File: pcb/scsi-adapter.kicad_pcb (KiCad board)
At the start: 4 copper layers, 0 parts

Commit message: basic pcb layout
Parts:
- added C1001: 22pF C0G, Capacitor_SMD:C_0402_1005Metric, F.Cu at (101.4, 209.3)
- added C1002: 100nF 50V, Capacitor_SMD:C_0402_1005Metric, F.Cu at (104.3, 209.3)
- added C101: 1uF 50V X7R, Capacitor_SMD:C_0805_2012Metric, F.Cu at (102.2, 173.0)
- added C102: 100nF 50V, Capacitor_SMD:C_0402_1005Metric, F.Cu at (105.9, 172.5)
- added C103: 2.2nF, Capacitor_SMD:C_0402_1005Metric, F.Cu at (108.8, 172.5)
- added C104: 1nF, Capacitor_SMD:C_0402_1005Metric, F.Cu at (111.6, 172.5)
- added C105: 1uF 25V, Capacitor_SMD:C_0402_1005Metric, F.Cu at (114.5, 172.5)
- added C106: 1uF 25V, Capacitor_SMD:C_0402_1005Metric, F.Cu at (117.4, 172.5)
- added C107: 4.7uF 25V, Capacitor_SMD:C_0805_2012Metric, F.Cu at (121.0, 173.0)
- added C108: 100nF 50V, Capacitor_SMD:C_0402_1005Metric, F.Cu at (124.7, 172.5)
- added C109: 22uF 25V, Capacitor_SMD:C_0805_2012Metric, F.Cu at (128.3, 173.0)
- added C110: 1uF 25V, Capacitor_SMD:C_0402_1005Metric, F.Cu at (132.0, 172.5)
- added C1101: 22pF C0G, Capacitor_SMD:C_0402_1005Metric, F.Cu at (107.2, 209.3)
- added C1102: 100nF 50V, Capacitor_SMD:C_0402_1005Metric, F.Cu at (110.0, 209.3)
- added C111: 10uF 25V, Capacitor_SMD:C_0805_2012Metric, F.Cu at (135.7, 173.0)
- added C112: 1uF 25V, Capacitor_SMD:C_0402_1005Metric, F.Cu at (139.3, 172.5)
- added C113: 10uF 25V, Capacitor_SMD:C_0805_2012Metric, F.Cu at (143.0, 173.0)
- added C1201: 22pF C0G, Capacitor_SMD:C_0402_1005Metric, F.Cu at (112.9, 209.3)
- added C1202: 100nF 50V, Capacitor_SMD:C_0402_1005Metric, F.Cu at (115.8, 209.3)
- added C1301: 22pF C0G, Capacitor_SMD:C_0402_1005Metric, F.Cu at (118.7, 209.3)
- added C1302: 100nF 50V, Capacitor_SMD:C_0402_1005Metric, F.Cu at (121.5, 209.3)
- added C1401: 22pF C0G, Capacitor_SMD:C_0402_1005Metric, F.Cu at (124.4, 209.3)
- added C1402: 100nF 50V, Capacitor_SMD:C_0402_1005Metric, F.Cu at (127.3, 209.3)
- added C1501: 22pF C0G, Capacitor_SMD:C_0402_1005Metric, F.Cu at (130.1, 209.3)
- added C1502: 100nF 50V, Capacitor_SMD:C_0402_1005Metric, F.Cu at (133.0, 209.3)
- added C1601: 22pF C0G, Capacitor_SMD:C_0402_1005Metric, F.Cu at (135.9, 209.3)
- added C1602: 100nF 50V, Capacitor_SMD:C_0402_1005Metric, F.Cu at (138.7, 209.3)
- added C1701: 22pF C0G, Capacitor_SMD:C_0402_1005Metric, F.Cu at (141.6, 209.3)
- added C1702: 100nF 50V, Capacitor_SMD:C_0402_1005Metric, F.Cu at (144.5, 209.3)
- added C1801: 22pF C0G, Capacitor_SMD:C_0402_1005Metric, F.Cu at (147.4, 209.3)
- added C1802: 100nF 50V, Capacitor_SMD:C_0402_1005Metric, F.Cu at (150.2, 209.3)
- added C1901: 22pF C0G, Capacitor_SMD:C_0402_1005Metric, F.Cu at (153.1, 209.3)
- added C1902: 100nF 50V, Capacitor_SMD:C_0402_1005Metric, F.Cu at (156.0, 209.3)
- added C2001: 22pF C0G, Capacitor_SMD:C_0402_1005Metric, F.Cu at (158.8, 209.3)
- added C2002: 100nF 50V, Capacitor_SMD:C_0402_1005Metric, F.Cu at (161.7, 209.3)
- added C201: 1uF 25V, Capacitor_SMD:C_0402_1005Metric, F.Cu at (101.4, 305.5)
- added C202: 1uF 25V, Capacitor_SMD:C_0402_1005Metric, F.Cu at (104.3, 305.5)
- added C203: 100nF 50V, Capacitor_SMD:C_0402_1005Metric, F.Cu at (107.2, 305.5)
- added C204: 2.2nF, Capacitor_SMD:C_0402_1005Metric, F.Cu at (110.0, 305.5)
- added C205: 1nF, Capacitor_SMD:C_0402_1005Metric, F.Cu at (112.9, 305.5)
- added C206: 100nF 50V, Capacitor_SMD:C_0402_1005Metric, F.Cu at (115.8, 305.5)
- added C207: 1uF 25V, Capacitor_SMD:C_0402_1005Metric, F.Cu at (118.7, 305.5)
- added C2101: 22pF C0G, Capacitor_SMD:C_0402_1005Metric, F.Cu at (164.6, 209.3)
- added C2102: 100nF 50V, Capacitor_SMD:C_0402_1005Metric, F.Cu at (167.4, 209.3)
- added C2202: 100nF 50V, Capacitor_SMD:C_0402_1005Metric, F.Cu at (170.3, 209.3)
- added C2301: 22pF C0G, Capacitor_SMD:C_0402_1005Metric, F.Cu at (173.2, 209.3)
- added C2302: 100nF 50V, Capacitor_SMD:C_0402_1005Metric, F.Cu at (176.1, 209.3)
- added C2402: 100nF 50V, Capacitor_SMD:C_0402_1005Metric, F.Cu at (178.9, 209.3)
- added C2502: 100nF 50V, Capacitor_SMD:C_0402_1005Metric, F.Cu at (181.8, 209.3)
- added C2602: 100nF 50V, Capacitor_SMD:C_0402_1005Metric, F.Cu at (184.7, 209.3)
- added C301: 100nF 50V, Capacitor_SMD:C_0402_1005Metric, F.Cu at (187.5, 209.3)
- added C302: 100nF 50V, Capacitor_SMD:C_0402_1005Metric, F.Cu at (190.4, 209.3)
- added C303: 100nF 50V, Capacitor_SMD:C_0402_1005Metric, F.Cu at (193.3, 209.3)
- added C401: 4.7uF 10V, Capacitor_SMD:C_0402_1005Metric, F.Cu at (146.0, 61.7)
- added C402: 4.7uF 10V, scsi-adapter:C_0402_1005Metric_Wide, F.Cu at (147.8, 63.0)
- added C403: 4.7uF 10V, scsi-adapter:C_0402_1005Metric_Wide, F.Cu at (147.2, 63.6)
- added C404: 4.7uF 10V, Capacitor_SMD:C_0402_1005Metric, F.Cu at (158.0, 52.8)
- added C405: 10uF 25V, Capacitor_SMD:C_0805_2012Metric, F.Cu at (140.1, 62.2)
- added C406: 100nF, Capacitor_SMD:C_0402_1005Metric, F.Cu at (157.9, 68.5)
- added C407: 100nF, Capacitor_SMD:C_0402_1005Metric, F.Cu at (161.5, 64.9)
- added C408: 100nF, Capacitor_SMD:C_0402_1005Metric, F.Cu at (162.3, 59.4)
- added C409: 100nF, Capacitor_SMD:C_0402_1005Metric, F.Cu at (161.0, 55.9)
- added C410: 100nF, Capacitor_SMD:C_0402_1005Metric, F.Cu at (152.1, 52.3)
- added C411: 100nF, Capacitor_SMD:C_0402_1005Metric, F.Cu at (148.9, 54.8)
- added C412: 100nF, Capacitor_SMD:C_0402_1005Metric, F.Cu at (145.9, 58.5)
- added C413: 100nF, Capacitor_SMD:C_0402_1005Metric, F.Cu at (152.6, 70.6)
- added C414: 100nF, Capacitor_SMD:C_0402_1005Metric, F.Cu at (159.8, 66.6)
- added C415: 100nF, Capacitor_SMD:C_0402_1005Metric, F.Cu at (159.1, 53.9)
- added C416: 100nF, Capacitor_SMD:C_0402_1005Metric, F.Cu at (148.2, 55.5)
- added C417: 100nF, Capacitor_SMD:C_0402_1005Metric, F.Cu at (146.6, 57.8)
- added C418: 100nF, Capacitor_SMD:C_0402_1005Metric, F.Cu at (148.7, 67.7)
- added C419: 15pF, Capacitor_SMD:C_0402_1005Metric, F.Cu at (162.6, 54.4)
- added C420: 15pF, Capacitor_SMD:C_0402_1005Metric, F.Cu at (160.5, 52.3)
- added C421: 100nF, Capacitor_SMD:C_0402_1005Metric, F.Cu at (143.9, 73.2)
- added C422: 100nF, Capacitor_SMD:C_0402_1005Metric, F.Cu at (139.9, 80.2)
- added C423: 1uF 25V, Capacitor_SMD:C_0402_1005Metric, F.Cu at (140.7, 80.9)
- added C424: 100nF, Capacitor_SMD:C_0402_1005Metric, F.Cu at (168.6, 191.0)
- added C501: 100nF, Capacitor_SMD:C_0402_1005Metric, F.Cu at (101.4, 148.3)
- added C502: 10uF 25V, Capacitor_SMD:C_0805_2012Metric, F.Cu at (105.1, 148.9)
- added C503: 100nF, Capacitor_SMD:C_0402_1005Metric, F.Cu at (108.8, 148.3)
- added C601: 10uF 25V, Capacitor_SMD:C_0805_2012Metric, F.Cu at (102.2, 319.1)
- added C602: 100nF, Capacitor_SMD:C_0402_1005Metric, F.Cu at (105.9, 318.6)
- added C603: 100nF, Capacitor_SMD:C_0402_1005Metric, F.Cu at (108.8, 318.6)
- added C604: DNP, Capacitor_SMD:C_0402_1005Metric, F.Cu at (111.6, 318.6)
- added C605: DNP, Capacitor_SMD:C_0402_1005Metric, F.Cu at (114.5, 318.6)
- added C701: 4.7uF 10V, Capacitor_SMD:C_0402_1005Metric, F.Cu at (101.4, 131.0)
- added C702: 100nF, Capacitor_SMD:C_0402_1005Metric, F.Cu at (104.3, 131.0)
- added C703: 4.7uF 10V, Capacitor_SMD:C_0402_1005Metric, F.Cu at (107.2, 131.0)
- added C704: 100nF, Capacitor_SMD:C_0402_1005Metric, F.Cu at (110.0, 131.0)
- added C705: 100nF, Capacitor_SMD:C_0402_1005Metric, F.Cu at (112.9, 131.0)
- added C706: 100nF, Capacitor_SMD:C_0402_1005Metric, F.Cu at (115.8, 131.0)
- added C707: 100nF, Capacitor_SMD:C_0402_1005Metric, F.Cu at (118.7, 131.0)
- added C708: 100nF, Capacitor_SMD:C_0402_1005Metric, F.Cu at (121.5, 131.0)
- added C709: 4.7uF, Capacitor_SMD:C_0402_1005Metric, F.Cu at (124.4, 131.0)
- added C710: 100nF, Capacitor_SMD:C_0402_1005Metric, F.Cu at (127.3, 131.0)
- added C711: 4.7uF, Capacitor_SMD:C_0402_1005Metric, F.Cu at (130.1, 131.0)
- added C712: 100nF, Capacitor_SMD:C_0402_1005Metric, F.Cu at (133.0, 131.0)
- added C713: 100nF, Capacitor_SMD:C_0402_1005Metric, F.Cu at (135.9, 131.0)
- added C714: 100nF, Capacitor_SMD:C_0402_1005Metric, F.Cu at (138.7, 131.0)
- added C715: 15pF, Capacitor_SMD:C_0402_1005Metric, F.Cu at (141.6, 131.0)
- added C716: 15pF, Capacitor_SMD:C_0402_1005Metric, F.Cu at (144.5, 131.0)
- added C717: 10nF, Capacitor_SMD:C_0402_1005Metric, F.Cu at (147.4, 131.0)
- added C901: 22pF C0G, Capacitor_SMD:C_0402_1005Metric, F.Cu at (196.1, 209.3)
- added C902: 100nF 50V, Capacitor_SMD:C_0402_1005Metric, F.Cu at (199.0, 209.3)
- added D101: SMF15CA, Diode_SMD:D_SOD-123F, F.Cu at (148.0, 173.2)
- added D102: BZT52C5V6, Diode_SMD:D_SOD-123, F.Cu at (153.6, 173.2)
- added D201: KT-0603R red, LED_SMD:LED_0603_1608Metric, F.Cu at (122.1, 305.8)
- added D202: KT-0805Y yellow, LED_SMD:LED_0805_2012Metric, F.Cu at (126.4, 306.0)
- added D203: SS14, Diode_SMD:D_SMA, F.Cu at (132.7, 306.8)
- added D204: SMF6.0A, Diode_SMD:D_SOD-123F, F.Cu at (139.5, 306.2)
- added D301: H5VUD5BB, Diode_SMD:D_SOD-523, F.Cu at (202.3, 209.5)
- added D302: H5VUD5BB, Diode_SMD:D_SOD-523, F.Cu at (205.9, 209.5)
- added D303: H5VUD5BB, Diode_SMD:D_SOD-523, F.Cu at (209.5, 209.5)
- added D304: H5VUD5BB, Diode_SMD:D_SOD-523, F.Cu at (213.1, 209.5)
- added D305: H5VUD5BB, Diode_SMD:D_SOD-523, F.Cu at (216.7, 209.5)
- added D306: H5VUD5BB, Diode_SMD:D_SOD-523, F.Cu at (220.2, 209.5)
- added D307: H5VUD5BB, Diode_SMD:D_SOD-523, F.Cu at (223.8, 209.5)
- added D308: H5VUD5BB, Diode_SMD:D_SOD-523, F.Cu at (227.4, 209.5)
- added D309: H5VUD5BB, Diode_SMD:D_SOD-523, F.Cu at (231.0, 209.5)
- added D310: H5VUD5BB, Diode_SMD:D_SOD-523, F.Cu at (234.6, 209.5)
- added D311: H5VUD5BB, Diode_SMD:D_SOD-523, F.Cu at (238.2, 209.5)
- added D312: H5VUD5BB, Diode_SMD:D_SOD-523, F.Cu at (241.8, 209.5)
- added D313: H5VUD5BB, Diode_SMD:D_SOD-523, F.Cu at (245.4, 209.5)
- added D314: H5VUD5BB, Diode_SMD:D_SOD-523, F.Cu at (249.0, 209.5)
- added D315: H5VUD5BB, Diode_SMD:D_SOD-523, F.Cu at (252.6, 209.5)
- added D316: H5VUD5BB, Diode_SMD:D_SOD-523, F.Cu at (256.2, 209.5)
- added D317: H5VUD5BB, Diode_SMD:D_SOD-523, F.Cu at (259.8, 209.5)
- added D318: H5VUD5BB, Diode_SMD:D_SOD-523, F.Cu at (263.4, 209.5)
- added D501: KT-0805Y yellow, LED_SMD:LED_0805_2012Metric, F.Cu at (112.4, 148.9)
- added D502: KT-0603R red, LED_SMD:LED_0603_1608Metric, F.Cu at (116.7, 148.6)
- added D503: KT-0603R red, LED_SMD:LED_0603_1608Metric, F.Cu at (120.7, 148.6)
- added D504: KT-0805Y yellow, LED_SMD:LED_0805_2012Metric, F.Cu at (125.0, 148.9)
- added D505: KT-0805G green, LED_SMD:LED_0805_2012Metric, F.Cu at (129.4, 148.9)
- added D601: H5VUD5BB, Diode_SMD:D_SOD-523, F.Cu at (117.8, 318.9)
- added D602: H5VUD5BB, Diode_SMD:D_SOD-523, F.Cu at (121.3, 318.9)
- added D603: H7VL10B, Diode_SMD:D_0402_1005Metric, F.Cu at (124.8, 318.6)
- added D604: H7VL10B, Diode_SMD:D_0402_1005Metric, F.Cu at (128.0, 318.6)
- added D605: SMF6.0A, Diode_SMD:D_SOD-123F, F.Cu at (132.2, 319.3)
- added D606: 1N5819WS, Diode_SMD:D_SOD-323, F.Cu at (137.1, 319.1)
- added D607: KT-0805G green, LED_SMD:LED_0805_2012Metric, F.Cu at (141.4, 319.1)
- added FB701: 600R@100MHz, Inductor_SMD:L_0603_1608Metric, F.Cu at (150.8, 131.3)
- added FB702: 600R@100MHz, Inductor_SMD:L_0603_1608Metric, F.Cu at (154.8, 131.3)
- added H1: M3, MountingHole_3.2mm_M3, F.Cu at (104.0, 34.0)
- added H2: M3, MountingHole_3.2mm_M3, F.Cu at (216.0, 34.0)
- added H3: M3, MountingHole_3.2mm_M3, F.Cu at (216.0, 116.0)
- added H4: M3, MountingHole_3.2mm_M3, F.Cu at (104.0, 116.0)
- added J101: Bench 5V, scsi-adapter:TerminalBlock_Kangnex_WJ500V-5.08-2P_1x02_P5.08mm_Horizontal, F.Cu at (105.5, 102.7)
- added J201: TERMPWR jumper, Connector_PinHeader_2.54mm:PinHeader_1x02_P2.54mm_Vertical, F.Cu at (136.0, 111.2)
- added J301: IDC50 box header, Connector_IDC:IDC-Header_2x25_P2.54mm_Vertical, F.Cu at (143.9, 114.3)
- added J302: HD50 female R/A, scsi-adapter:TE_AMPLIMITE-050_5787082-5_50pos_P1.27mm_Horizontal, F.Cu at (210.6, 59.8)
- added J303: 2x17 box header, Connector_IDC:IDC-Header_2x17_P2.54mm_Vertical, F.Cu at (204.9, 35.7)
- added J401: TC2030-IDC, Connector:Tag-Connect_TC2030-IDC-FP_2x03_P1.27mm_Vertical, F.Cu at (149.5, 39.0)
- added J501: TF PUSH, scsi-adapter:microSD_SHOUHAN_TF-PUSH_PushPush_CardDetect, F.Cu at (127.5, 34.0)
- added J601: USB-C (HRO TYPE-C-31-M-12), Connector_USB:USB_C_Receptacle_HRO_TYPE-C-31-M-12, F.Cu at (103.2, 75.0)
- added L401: 3.3uH, scsi-adapter:L_Abracon_AOTA-B201610_2.0x1.6mm_Polarized, F.Cu at (146.0, 64.8)
- added Q1001: FDV301N, Package_TO_SOT_SMD:SOT-23, F.Cu at (65.4, 151.9)
- added Q1101: FDV301N, Package_TO_SOT_SMD:SOT-23, F.Cu at (102.5, 283.7)
- added Q1201: FDV301N, Package_TO_SOT_SMD:SOT-23, F.Cu at (107.4, 283.7)
- added Q1301: FDV301N, Package_TO_SOT_SMD:SOT-23, F.Cu at (112.3, 283.7)
- added Q1401: FDV301N, Package_TO_SOT_SMD:SOT-23, F.Cu at (117.2, 283.7)
- added Q1501: FDV301N, Package_TO_SOT_SMD:SOT-23, F.Cu at (122.1, 283.7)
- added Q1601: FDV301N, Package_TO_SOT_SMD:SOT-23, F.Cu at (127.0, 283.7)
- added Q1701: FDV301N, Package_TO_SOT_SMD:SOT-23, F.Cu at (131.9, 283.7)
- added Q1801: FDV301N, Package_TO_SOT_SMD:SOT-23, F.Cu at (136.8, 283.7)
- added Q1901: FDV301N, Package_TO_SOT_SMD:SOT-23, F.Cu at (141.7, 283.7)
- added Q2001: FDV301N, Package_TO_SOT_SMD:SOT-23, F.Cu at (146.6, 283.7)
- added Q201: 2N7002, Package_TO_SOT_SMD:SOT-23, F.Cu at (149.2, 306.7)
- added Q2101: FDV301N, Package_TO_SOT_SMD:SOT-23, F.Cu at (151.6, 283.7)
- added Q2301: FDV301N, Package_TO_SOT_SMD:SOT-23, F.Cu at (156.5, 283.7)
- added Q901: FDV301N, Package_TO_SOT_SMD:SOT-23, F.Cu at (161.4, 283.7)
- added R1001: 100R, Resistor_SMD:R_0402_1005Metric, F.Cu at (165.3, 282.5)
- added R1002: 4.7k, Resistor_SMD:R_0402_1005Metric, F.Cu at (168.2, 282.5)
- added R1003: 100R, Resistor_SMD:R_0402_1005Metric, F.Cu at (171.1, 282.5)
- added R101: 510k, Resistor_SMD:R_0402_1005Metric, F.Cu at (170.8, 172.5)
- added R102: 39k, Resistor_SMD:R_0402_1005Metric, F.Cu at (173.7, 172.5)
- added R103: 3.9k, Resistor_SMD:R_0402_1005Metric, F.Cu at (176.6, 172.5)
- added R104: 150k, Resistor_SMD:R_0402_1005Metric, F.Cu at (179.5, 172.5)
- added R105: 10k, Resistor_SMD:R_0402_1005Metric, F.Cu at (182.4, 172.5)
- added R106: 1.5k, Resistor_SMD:R_0402_1005Metric, F.Cu at (185.3, 172.5)
- added R107: 100k, Resistor_SMD:R_0402_1005Metric, F.Cu at (188.2, 172.5)
- added R108: 39k, Resistor_SMD:R_0402_1005Metric, F.Cu at (191.1, 172.5)
- added R109: 10k, Resistor_SMD:R_0402_1005Metric, F.Cu at (194.0, 172.5)
- added R110: 1R, Resistor_SMD:R_0603_1608Metric, F.Cu at (197.5, 172.7)
- added R1101: 100R, Resistor_SMD:R_0402_1005Metric, F.Cu at (174.0, 282.5)
- added R1102: 4.7k, Resistor_SMD:R_0402_1005Metric, F.Cu at (176.9, 282.5)
- added R1103: 100R, Resistor_SMD:R_0402_1005Metric, F.Cu at (179.8, 282.5)
- added R111: 100k, Resistor_SMD:R_0402_1005Metric, F.Cu at (201.0, 172.5)
- added R112: 75k, Resistor_SMD:R_0402_1005Metric, F.Cu at (203.9, 172.5)
- added R113: 47k, Resistor_SMD:R_0402_1005Metric, F.Cu at (206.8, 172.5)
- added R114: 27k, Resistor_SMD:R_0402_1005Metric, F.Cu at (209.7, 172.5)
- added R115: 1M, Resistor_SMD:R_0603_1608Metric, F.Cu at (213.2, 172.7)
- added R116: 100k, Resistor_SMD:R_0402_1005Metric, F.Cu at (216.6, 172.5)
- added R117: 75k, Resistor_SMD:R_0402_1005Metric, F.Cu at (219.5, 172.5)
- added R118: 39k, Resistor_SMD:R_0402_1005Metric, F.Cu at (222.4, 172.5)
- added R119: 5.6k, Resistor_SMD:R_0402_1005Metric, F.Cu at (225.3, 172.5)
- added R120: 33k, Resistor_SMD:R_0402_1005Metric, F.Cu at (228.3, 172.5)
- added R1201: 100R, Resistor_SMD:R_0402_1005Metric, F.Cu at (182.7, 282.5)
- added R1202: 4.7k, Resistor_SMD:R_0402_1005Metric, F.Cu at (185.7, 282.5)
- added R1203: 100R, Resistor_SMD:R_0402_1005Metric, F.Cu at (188.6, 282.5)
- added R121: 270R, Resistor_SMD:R_0603_1608Metric, F.Cu at (231.7, 172.7)
- added R1301: 100R, Resistor_SMD:R_0402_1005Metric, F.Cu at (191.5, 282.5)
- added R1302: 4.7k, Resistor_SMD:R_0402_1005Metric, F.Cu at (194.4, 282.5)
- added R1303: 100R, Resistor_SMD:R_0402_1005Metric, F.Cu at (197.3, 282.5)
- added R1401: 100R, Resistor_SMD:R_0402_1005Metric, F.Cu at (200.2, 282.5)
- added R1402: 4.7k, Resistor_SMD:R_0402_1005Metric, F.Cu at (203.1, 282.5)
- added R1403: 100R, Resistor_SMD:R_0402_1005Metric, F.Cu at (206.0, 282.5)
- added R1501: 100R, Resistor_SMD:R_0402_1005Metric, F.Cu at (208.9, 282.5)
- added R1502: 4.7k, Resistor_SMD:R_0402_1005Metric, F.Cu at (211.8, 282.5)
- added R1503: 100R, Resistor_SMD:R_0402_1005Metric, F.Cu at (214.8, 282.5)
- added R1601: 100R, Resistor_SMD:R_0402_1005Metric, F.Cu at (217.7, 282.5)
- added R1602: 4.7k, Resistor_SMD:R_0402_1005Metric, F.Cu at (220.6, 282.5)
- added R1603: 100R, Resistor_SMD:R_0402_1005Metric, F.Cu at (223.5, 282.5)
- added R1701: 100R, Resistor_SMD:R_0402_1005Metric, F.Cu at (226.4, 282.5)
- added R1702: 4.7k, Resistor_SMD:R_0402_1005Metric, F.Cu at (229.3, 282.5)
- added R1703: 100R, Resistor_SMD:R_0402_1005Metric, F.Cu at (232.2, 282.5)
- added R1801: 100R, Resistor_SMD:R_0402_1005Metric, F.Cu at (235.1, 282.5)
- added R1802: 4.7k, Resistor_SMD:R_0402_1005Metric, F.Cu at (238.0, 282.5)
- added R1803: 100R, Resistor_SMD:R_0402_1005Metric, F.Cu at (240.9, 282.5)
- added R1901: 100R, Resistor_SMD:R_0402_1005Metric, F.Cu at (243.9, 282.5)
- added R1902: 4.7k, Resistor_SMD:R_0402_1005Metric, F.Cu at (246.8, 282.5)
- added R1903: 100R, Resistor_SMD:R_0402_1005Metric, F.Cu at (249.7, 282.5)
- added R2001: 100R, Resistor_SMD:R_0402_1005Metric, F.Cu at (252.6, 282.5)
- added R2002: 4.7k, Resistor_SMD:R_0402_1005Metric, F.Cu at (255.5, 282.5)
- added R2003: 100R, Resistor_SMD:R_0402_1005Metric, F.Cu at (258.4, 282.5)
- added R201: 10k, Resistor_SMD:R_0402_1005Metric, F.Cu at (153.1, 305.5)
- added R202: 10k, Resistor_SMD:R_0402_1005Metric, F.Cu at (156.0, 305.5)
- added R203: 470R, Resistor_SMD:R_0402_1005Metric, F.Cu at (159.0, 305.5)
- added R204: 10k, Resistor_SMD:R_0402_1005Metric, F.Cu at (161.9, 305.5)
- added R205: 3.3k, Resistor_SMD:R_0402_1005Metric, F.Cu at (164.8, 305.5)
- added R206: 4.7k, Resistor_SMD:R_0402_1005Metric, F.Cu at (167.7, 305.5)
- added R207: 1M, Resistor_SMD:R_0402_1005Metric, F.Cu at (170.6, 305.5)
- added R208: 10k, Resistor_SMD:R_0402_1005Metric, F.Cu at (173.5, 305.5)
- added R209: 1k, Resistor_SMD:R_0402_1005Metric, F.Cu at (176.4, 305.5)
- added R210: 10k, Resistor_SMD:R_0402_1005Metric, F.Cu at (179.3, 305.5)
- added R2101: 100R, Resistor_SMD:R_0402_1005Metric, F.Cu at (261.3, 282.5)
- added R2102: 4.7k, Resistor_SMD:R_0402_1005Metric, F.Cu at (264.2, 282.5)
- added R2103: 100R, Resistor_SMD:R_0402_1005Metric, F.Cu at (267.1, 282.5)
- added R211: 100k, Resistor_SMD:R_0402_1005Metric, F.Cu at (182.2, 305.5)
- added R212: 10k, Resistor_SMD:R_0402_1005Metric, F.Cu at (185.1, 305.5)
- added R213: 39k, Resistor_SMD:R_0402_1005Metric, F.Cu at (188.1, 305.5)
- added R214: 15k, Resistor_SMD:R_0402_1005Metric, F.Cu at (191.0, 305.5)
- added R215: 56k, Resistor_SMD:R_0402_1005Metric, F.Cu at (193.9, 305.5)
- added R216: 47k, Resistor_SMD:R_0402_1005Metric, F.Cu at (196.8, 305.5)
- added R217: 2.4k, Resistor_SMD:R_0402_1005Metric, F.Cu at (199.7, 305.5)
- added R218: 330R, Resistor_SMD:R_0402_1005Metric, F.Cu at (202.6, 305.5)
- added R2203: 100R, Resistor_SMD:R_0402_1005Metric, F.Cu at (270.0, 282.5)
- added R2301: 100R, Resistor_SMD:R_0402_1005Metric, F.Cu at (273.0, 282.5)
- added R2302: 4.7k, Resistor_SMD:R_0402_1005Metric, F.Cu at (275.9, 282.5)
- added R2303: 100R, Resistor_SMD:R_0402_1005Metric, F.Cu at (278.8, 282.5)
- added R2403: 100R, Resistor_SMD:R_0402_1005Metric, F.Cu at (281.7, 282.5)
- added R2503: 100R, Resistor_SMD:R_0402_1005Metric, F.Cu at (284.6, 282.5)
- added R2603: 100R, Resistor_SMD:R_0402_1005Metric, F.Cu at (287.5, 282.5)
- added R301: 220R, Resistor_SMD:R_0402_1005Metric, F.Cu at (290.4, 282.5)
- added R302: 220R, Resistor_SMD:R_0402_1005Metric, F.Cu at (293.3, 282.5)
- added R303: 220R, Resistor_SMD:R_0402_1005Metric, F.Cu at (296.2, 282.5)
- added R304: 220R, Resistor_SMD:R_0402_1005Metric, F.Cu at (299.1, 282.5)
- added R305: 220R, Resistor_SMD:R_0402_1005Metric, F.Cu at (302.1, 282.5)
- added R306: 220R, Resistor_SMD:R_0402_1005Metric, F.Cu at (305.0, 282.5)
- added R307: 220R, Resistor_SMD:R_0402_1005Metric, F.Cu at (307.9, 282.5)
- added R308: 220R, Resistor_SMD:R_0402_1005Metric, F.Cu at (310.8, 282.5)
- added R309: 220R, Resistor_SMD:R_0402_1005Metric, F.Cu at (313.7, 282.5)
- added R310: 220R, Resistor_SMD:R_0402_1005Metric, F.Cu at (316.6, 282.5)
- added R311: 220R, Resistor_SMD:R_0402_1005Metric, F.Cu at (319.5, 282.5)
- added R312: 220R, Resistor_SMD:R_0402_1005Metric, F.Cu at (322.4, 282.5)
- added R313: 220R, Resistor_SMD:R_0402_1005Metric, F.Cu at (325.3, 282.5)
- added R314: 220R, Resistor_SMD:R_0402_1005Metric, F.Cu at (328.2, 282.5)
- added R315: 220R, Resistor_SMD:R_0402_1005Metric, F.Cu at (331.2, 282.5)
- added R316: 220R, Resistor_SMD:R_0402_1005Metric, F.Cu at (334.1, 282.5)
- added R317: 220R, Resistor_SMD:R_0402_1005Metric, F.Cu at (337.0, 282.5)
- added R318: 220R, Resistor_SMD:R_0402_1005Metric, F.Cu at (339.9, 282.5)
- added R319: 220R, Resistor_SMD:R_0402_1005Metric, F.Cu at (342.8, 282.5)
- added R320: 220R, Resistor_SMD:R_0402_1005Metric, F.Cu at (345.7, 282.5)
- added R321: 220R, Resistor_SMD:R_0402_1005Metric, F.Cu at (101.5, 286.9)
- added R322: 220R, Resistor_SMD:R_0402_1005Metric, F.Cu at (104.4, 286.9)
- added R323: 220R, Resistor_SMD:R_0402_1005Metric, F.Cu at (107.3, 286.9)
- added R324: 220R, Resistor_SMD:R_0402_1005Metric, F.Cu at (110.2, 286.9)
- added R325: 220R, Resistor_SMD:R_0402_1005Metric, F.Cu at (113.1, 286.9)
- added R326: 220R, Resistor_SMD:R_0402_1005Metric, F.Cu at (116.0, 286.9)
- added R327: 220R, Resistor_SMD:R_0402_1005Metric, F.Cu at (118.9, 286.9)
- added R328: 220R, Resistor_SMD:R_0402_1005Metric, F.Cu at (121.8, 286.9)
- added R329: 220R, Resistor_SMD:R_0402_1005Metric, F.Cu at (124.7, 286.9)
- added R330: 220R, Resistor_SMD:R_0402_1005Metric, F.Cu at (127.6, 286.9)
- added R331: 220R, Resistor_SMD:R_0402_1005Metric, F.Cu at (130.6, 286.9)
- added R332: 220R, Resistor_SMD:R_0402_1005Metric, F.Cu at (133.5, 286.9)
- added R333: 220R, Resistor_SMD:R_0402_1005Metric, F.Cu at (136.4, 286.9)
- added R334: 220R, Resistor_SMD:R_0402_1005Metric, F.Cu at (139.3, 286.9)
- added R335: 220R, Resistor_SMD:R_0402_1005Metric, F.Cu at (142.2, 286.9)
- added R336: 220R, Resistor_SMD:R_0402_1005Metric, F.Cu at (145.1, 286.9)
- added R337: 0R, Resistor_SMD:R_0402_1005Metric, F.Cu at (148.0, 286.9)
- added R338: 0R, Resistor_SMD:R_0402_1005Metric, F.Cu at (150.9, 286.9)
- added R339: 0R, Resistor_SMD:R_0402_1005Metric, F.Cu at (153.8, 286.9)
- added R340: 0R, Resistor_SMD:R_0402_1005Metric, F.Cu at (156.7, 286.9)
- added R341: 10k, Resistor_SMD:R_0402_1005Metric, F.Cu at (159.7, 286.9)
- added R342: 1k, Resistor_SMD:R_0402_1005Metric, F.Cu at (162.6, 286.9)
- added R343: 0R, Resistor_SMD:R_0402_1005Metric, F.Cu at (165.5, 286.9)
- added R401: 33R, Resistor_SMD:R_0402_1005Metric, F.Cu at (144.7, 63.0)
- added R402: 1k, Resistor_SMD:R_0402_1005Metric, F.Cu at (160.0, 54.8)
- added R403: 3.3k, Resistor_SMD:R_0402_1005Metric, F.Cu at (143.9, 84.4)
- added R404: 10k, Resistor_SMD:R_0402_1005Metric, F.Cu at (150.4, 81.2)
- added R405: 1k, Resistor_SMD:R_0402_1005Metric, F.Cu at (151.2, 81.9)
- added R406: 1k, Resistor_SMD:R_0402_1005Metric, F.Cu at (152.4, 47.2)
- added R407: 33R, Resistor_SMD:R_0402_1005Metric, F.Cu at (201.7, 191.0)
- added R408: 33R, Resistor_SMD:R_0402_1005Metric, F.Cu at (204.6, 191.0)
- added R409: 33R, Resistor_SMD:R_0402_1005Metric, F.Cu at (207.5, 191.0)
- added R410: 33R, Resistor_SMD:R_0402_1005Metric, F.Cu at (210.4, 191.0)
- added R411: 33R, Resistor_SMD:R_0402_1005Metric, F.Cu at (213.3, 191.0)
- added R412: 33R, Resistor_SMD:R_0402_1005Metric, F.Cu at (216.2, 191.0)
- added R413: 33R, Resistor_SMD:R_0402_1005Metric, F.Cu at (219.1, 191.0)
- added R414: 100R, Resistor_SMD:R_0402_1005Metric, F.Cu at (222.0, 191.0)
- added R415: 100R, Resistor_SMD:R_0402_1005Metric, F.Cu at (224.9, 191.0)
- added R416: 27R, Resistor_SMD:R_0603_1608Metric, F.Cu at (146.3, 68.7)
- added R417: 27R, Resistor_SMD:R_0603_1608Metric, F.Cu at (145.3, 67.7)
- added R418: 0R, Resistor_SMD:R_0402_1005Metric, F.Cu at (235.9, 191.0)
- added R419: 0R, Resistor_SMD:R_0402_1005Metric, F.Cu at (238.8, 191.0)
- added R420: 0R, Resistor_SMD:R_0402_1005Metric, F.Cu at (241.7, 191.0)
- added R421: 0R, Resistor_SMD:R_0402_1005Metric, F.Cu at (244.6, 191.0)
- added R422: 0R, Resistor_SMD:R_0402_1005Metric, F.Cu at (247.5, 191.0)
- added R423: 0R, Resistor_SMD:R_0402_1005Metric, F.Cu at (250.4, 191.0)
- added R424: 0R, Resistor_SMD:R_0402_1005Metric, F.Cu at (253.3, 191.0)
- added R425: 0R, Resistor_SMD:R_0402_1005Metric, F.Cu at (256.2, 191.0)
- added R426: 0R, Resistor_SMD:R_0402_1005Metric, F.Cu at (259.1, 191.0)
- added R427: 0R, Resistor_SMD:R_0402_1005Metric, F.Cu at (262.1, 191.0)
- added R428: 100k, Resistor_SMD:R_0402_1005Metric, F.Cu at (265.0, 191.0)
- added R429: 100k, Resistor_SMD:R_0402_1005Metric, F.Cu at (267.9, 191.0)
- added R501: 4.7k, Resistor_SMD:R_0402_1005Metric, F.Cu at (151.3, 148.3)
- added R502: 4.7k, Resistor_SMD:R_0402_1005Metric, F.Cu at (154.3, 148.3)
- added R503: 10k, Resistor_SMD:R_0402_1005Metric, F.Cu at (157.2, 148.3)
- added R504: 1k, Resistor_SMD:R_0402_1005Metric, F.Cu at (160.1, 148.3)
- added R505: 1k, Resistor_SMD:R_0402_1005Metric, F.Cu at (163.0, 148.3)
- added R506: 10k, Resistor_SMD:R_0402_1005Metric, F.Cu at (165.9, 148.3)
- added R507: 10k, Resistor_SMD:R_0402_1005Metric, F.Cu at (168.8, 148.3)
- added R508: 10k, Resistor_SMD:R_0402_1005Metric, F.Cu at (171.7, 148.3)
- added R509: 10k, Resistor_SMD:R_0402_1005Metric, F.Cu at (174.6, 148.3)
- added R510: 10k, Resistor_SMD:R_0402_1005Metric, F.Cu at (177.5, 148.3)
- added R511: 1k, Resistor_SMD:R_0402_1005Metric, F.Cu at (180.4, 148.3)
- added R512: 1k, Resistor_SMD:R_0402_1005Metric, F.Cu at (183.4, 148.3)
- added R513: 470R, Resistor_SMD:R_0402_1005Metric, F.Cu at (186.3, 148.3)
- added R601: 5.1k, Resistor_SMD:R_0402_1005Metric, F.Cu at (156.8, 318.6)
- added R602: 5.1k, Resistor_SMD:R_0402_1005Metric, F.Cu at (159.7, 318.6)
- added R603: 0R, Resistor_SMD:R_0402_1005Metric, F.Cu at (162.6, 318.6)
- added R604: 470R, Resistor_SMD:R_0402_1005Metric, F.Cu at (165.5, 318.6)
- added R701: 12k 1%, Resistor_SMD:R_0402_1005Metric, F.Cu at (158.3, 131.0)
- added R702: 10k, Resistor_SMD:R_0402_1005Metric, F.Cu at (161.2, 131.0)
- added R703: 10k, Resistor_SMD:R_0402_1005Metric, F.Cu at (164.1, 131.0)
- added R704: 2.2k, Resistor_SMD:R_0402_1005Metric, F.Cu at (167.0, 131.0)
- added R705: 10k, Resistor_SMD:R_0402_1005Metric, F.Cu at (169.9, 131.0)
- added R706: 10k, Resistor_SMD:R_0402_1005Metric, F.Cu at (172.8, 131.0)
- added R901: 100R, Resistor_SMD:R_0402_1005Metric, F.Cu at (168.4, 286.9)
- added R902: 4.7k, Resistor_SMD:R_0402_1005Metric, F.Cu at (171.3, 286.9)
- added R903: 100R, Resistor_SMD:R_0402_1005Metric, F.Cu at (174.2, 286.9)
- added SW301: DIP 2-pos, scsi-adapter:SW_DIP_SPSTx02_Slide_SHOUHAN_2.54-2P-TPGT_W8.8mm_P2.54mm, F.Cu at (124.2, 79.5)
- added SW401: BOOTSEL, Button_Switch_THT:SW_PUSH_6mm, F.Cu at (121.0, 88.2)
- added SW402: RUN, Button_Switch_THT:SW_PUSH_6mm, F.Cu at (120.5, 97.2)
- added TP101: BENCH+, TestPoint:TestPoint_Loop_D2.50mm_Drill1.0mm, F.Cu at (236.0, 173.8)
- added TP102: GND, TestPoint:TestPoint_Loop_D2.50mm_Drill1.0mm, F.Cu at (240.7, 173.8)
- added TP501: INT, TestPoint:TestPoint_Pad_D1.5mm, F.Cu at (189.5, 149.1)
- added TP502: +5V_SYS, TestPoint:TestPoint_Pad_D1.5mm, F.Cu at (193.0, 149.1)
- added TP503: +3V3, TestPoint:TestPoint_Pad_D1.5mm, F.Cu at (196.6, 149.1)
- added TP504: VTERM, TestPoint:TestPoint_Pad_D1.5mm, F.Cu at (200.1, 149.1)
- added TP505: TERMPWR, TestPoint:TestPoint_Pad_D1.5mm, F.Cu at (203.7, 149.1)
- added TP506: TP_EN, TestPoint:TestPoint_Pad_D1.5mm, F.Cu at (207.2, 149.1)
- added TP507: GND, TestPoint:TestPoint_Pad_D1.5mm, F.Cu at (210.8, 149.1)
- added TP508: P15, TestPoint:TestPoint_Pad_D1.5mm, F.Cu at (214.3, 149.1)
- added TP509: P16, TestPoint:TestPoint_Pad_D1.5mm, F.Cu at (217.9, 149.1)
- added TP510: P17, TestPoint:TestPoint_Pad_D1.5mm, F.Cu at (221.4, 149.1)
- added TP701: FT232H_3V3, TestPoint:TestPoint_Pad_D1.5mm, F.Cu at (176.0, 131.8)
- added U1001: 74LVC1G17GW, Package_TO_SOT_SMD:SOT-353_SC-70-5, F.Cu at (187.0, 287.8)
- added U101: TPS259470ARPWR, scsi-adapter:Texas_RPW0010A_VQFN-HR-10_2x2mm_P0.45mm, F.Cu at (115.2, 107.9)
- added U102: TPS2116DRLR, Package_TO_SOT_SMD:SOT-583-8, F.Cu at (105.7, 87.0)
- added U103: TPS73701DCQR, Package_TO_SOT_SMD:SOT-223-6, F.Cu at (116.5, 114.5)
- added U104: TPS73701DCQR, Package_TO_SOT_SMD:SOT-223-6, F.Cu at (195.0, 88.5)
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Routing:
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- added copper zone on F.Cu, net +3V3
- added copper zone on In2.Cu, net +3V3
- added copper zone on F.Cu, net /rp2350/DVDD_1V1
- added copper zone on F.Cu, net /rp2350/VREG_LX
- added copper zone on F.Cu, net GND
- added copper zone on In1.Cu, net GND
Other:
- board outline added: 120 x 90 mm

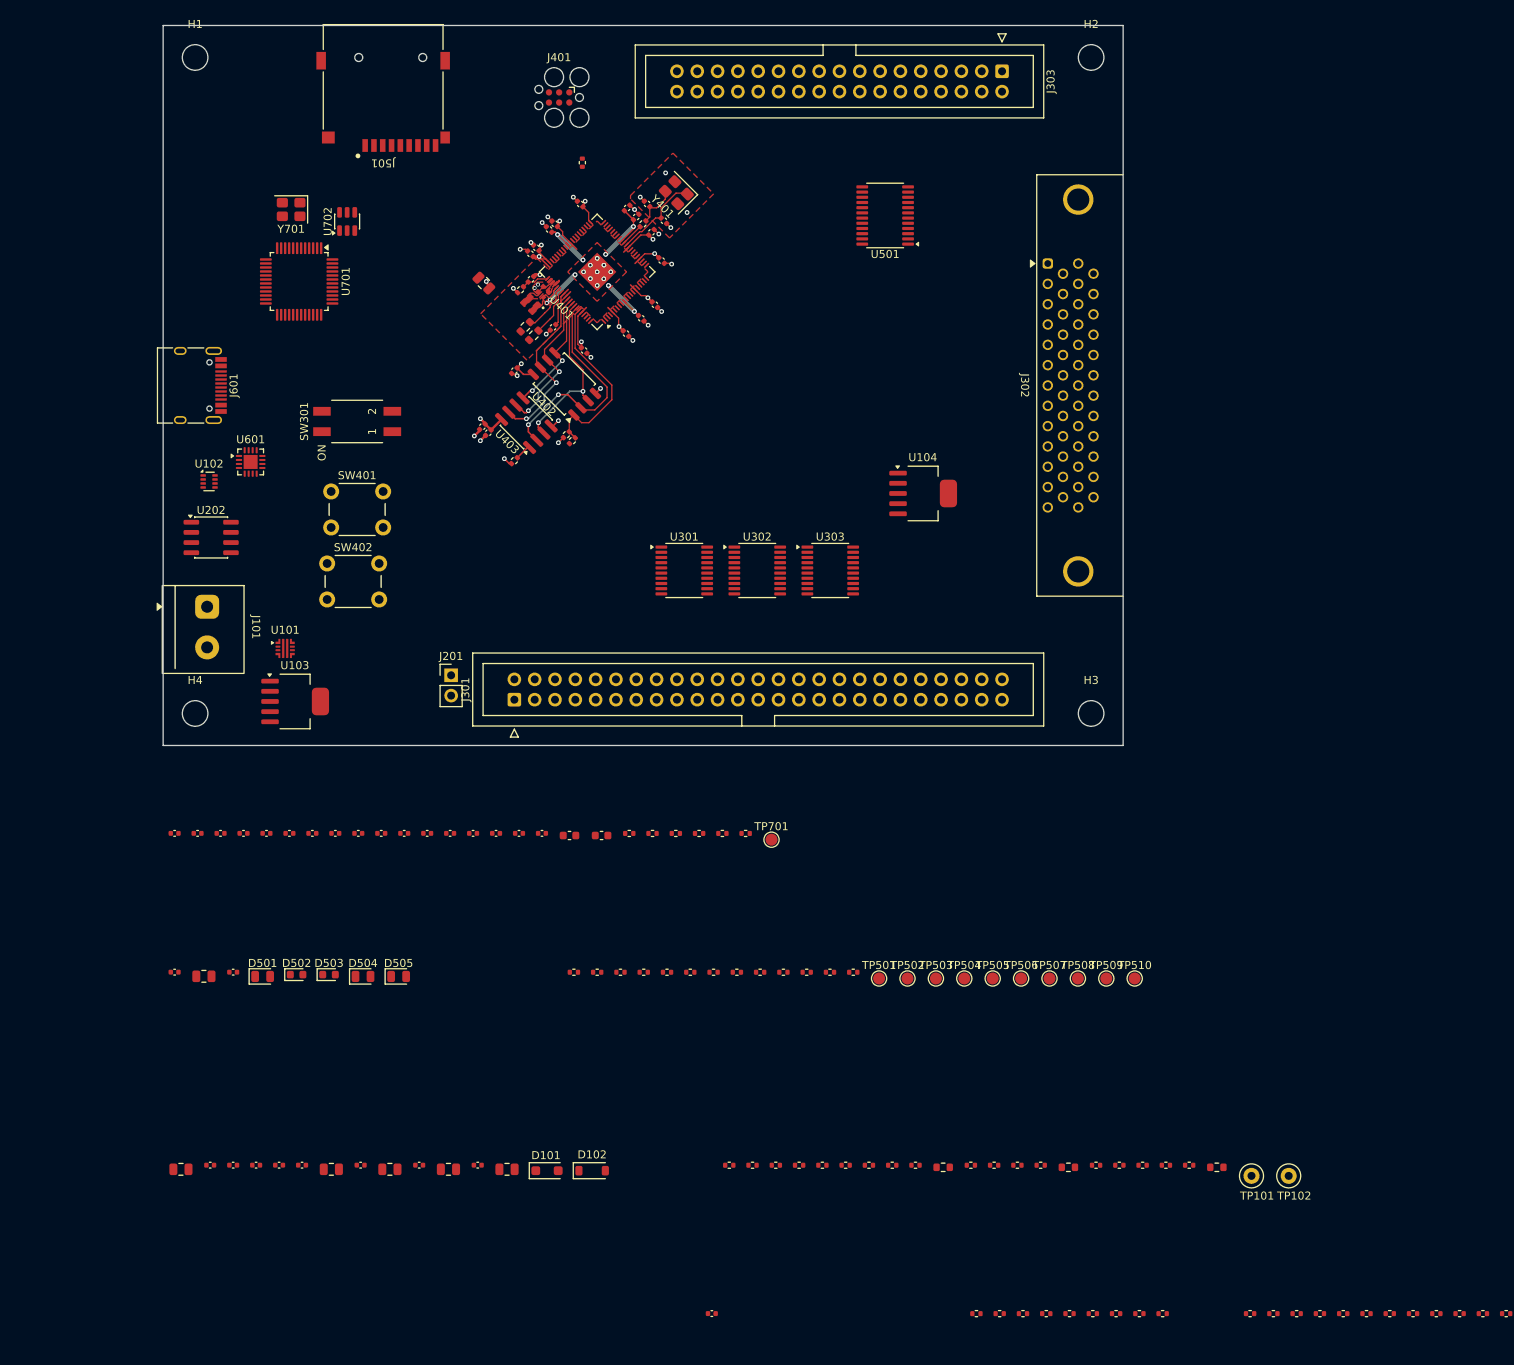
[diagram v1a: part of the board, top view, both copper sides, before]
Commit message: start routing ft232h
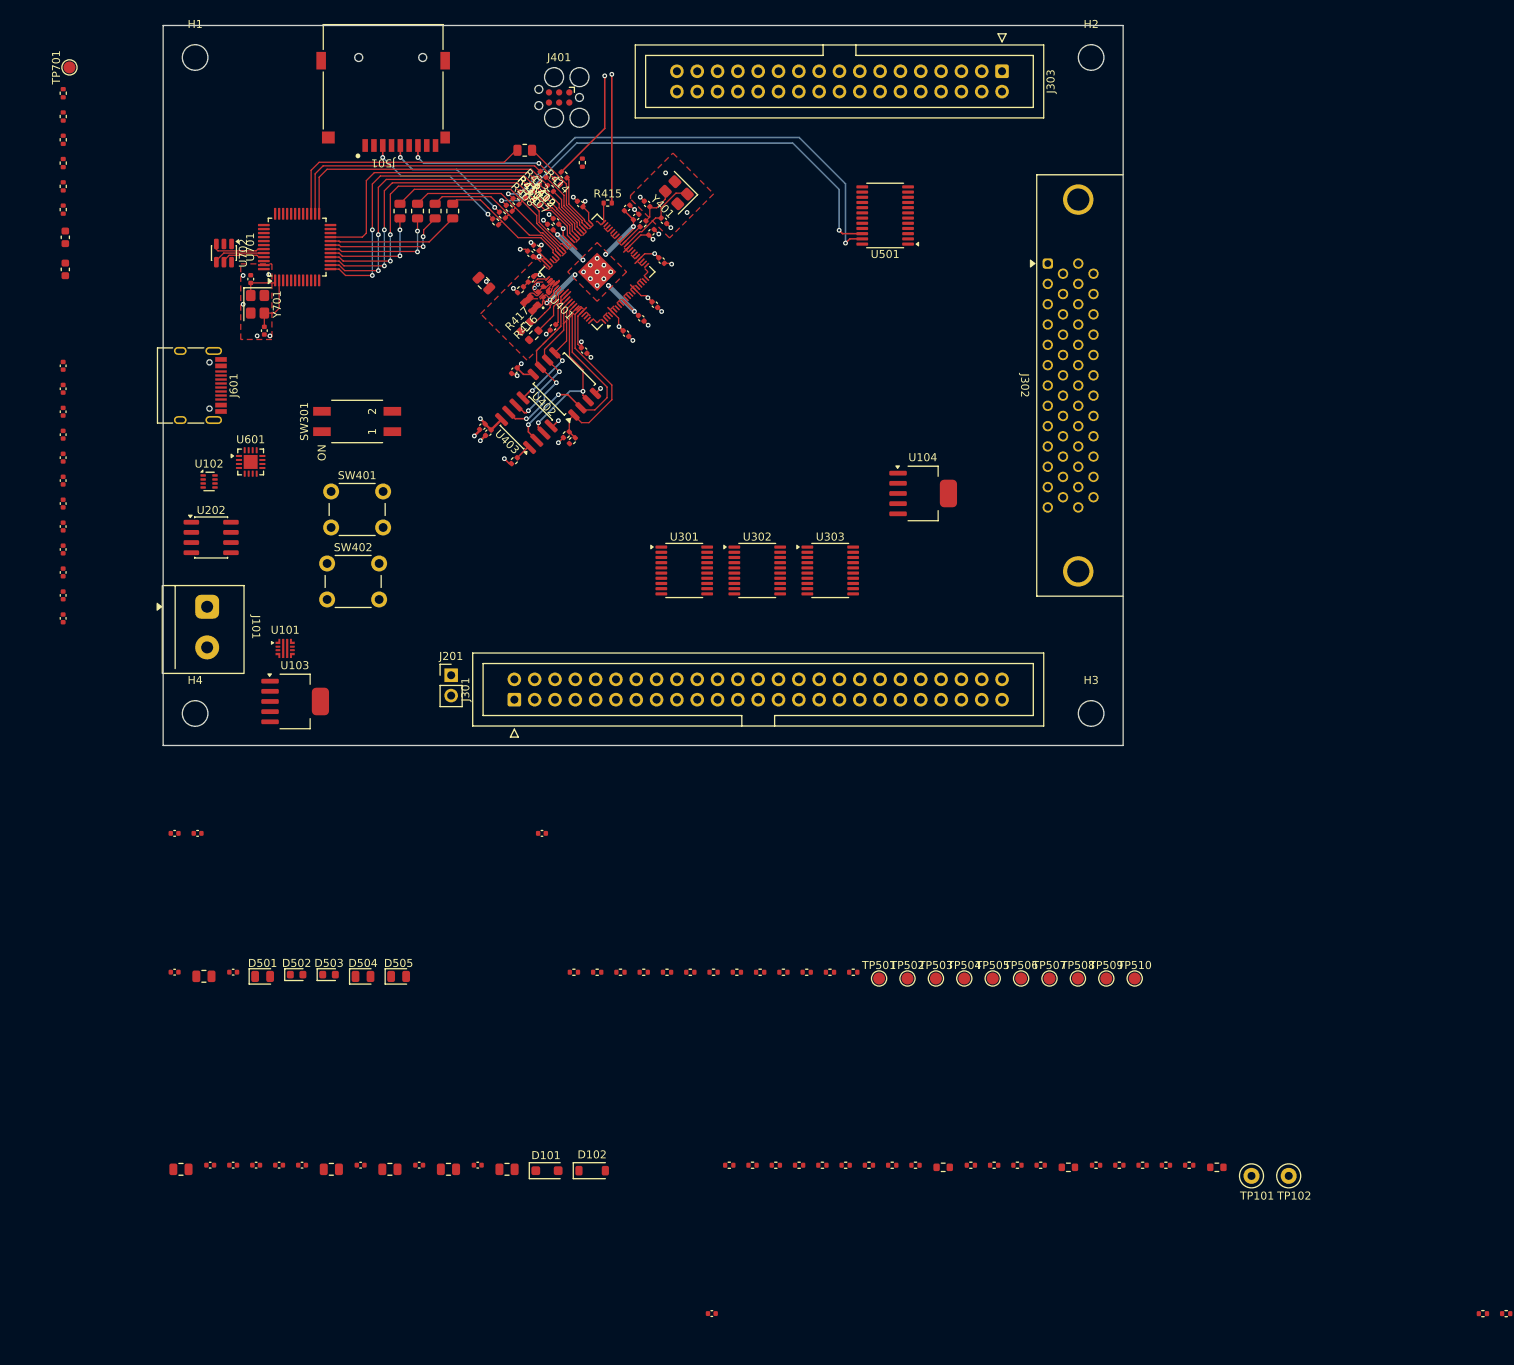
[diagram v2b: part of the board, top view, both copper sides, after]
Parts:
- R419, R421, R423, R425, R427: footprint Resistor_SMD:R_0402_1005Metric -> Resistor_SMD:R_0805_2012Metric
- moved R427 186.6 mm to (145.2, 45.6), turned to 180 degrees
- moved R425 182.8 mm to (136.2, 53.2), turned to -90 degrees
- moved R423 180.4 mm to (134.0, 53.2), turned to -90 degrees
- moved R426 179.2 mm to (149.3, 49.5), turned to 135 degrees
- moved R421 178.1 mm to (131.8, 53.2), turned to -90 degrees
- moved R424 176.4 mm to (141.6, 54.5), turned to 135 degrees
- moved R419 175.8 mm to (129.6, 53.2), turned to -90 degrees
- moved R422 172.9 mm to (142.4, 53.7), turned to 135 degrees
- moved R420 169.6 mm to (143.3, 52.8), turned to 135 degrees
- moved R418 166.6 mm to (144.1, 52.0), turned to 135 degrees
- moved R414 159.5 mm to (150.1, 48.7), turned to 135 degrees
- moved R413 159.4 mm to (147.5, 48.6), turned to 135 degrees
- moved R411 156.5 mm to (146.6, 49.5), turned to 135 degrees
- moved R412 156.1 mm to (148.4, 50.4), turned to 135 degrees
- moved R415 155.2 mm to (155.6, 52.2)
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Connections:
- R407 pad 1: Net-(U401-GPIO32) -> Net-(U401-GPIO38)
- R408 pad 1: Net-(U401-GPIO33) -> Net-(U401-GPIO39)
- R409 pad 1: Net-(U401-GPIO34) -> /FT232H_MIOSIO2
- R409 pad 2: /FT232H_MIOSIO2 -> Net-(U401-GPIO40/ADC0)
- R410 pad 1: Net-(U401-GPIO35) -> /FT232H_MIOSIO3
- R410 pad 2: /FT232H_MIOSIO3 -> Net-(U401-GPIO41/ADC1)
- R411 pad 1: /FT232H_SCLK -> Net-(U401-GPIO37)
- R411 pad 2: Net-(U401-GPIO41/ADC1) -> /FT232H_SCLK
- R412 pad 1: /FT232H_SS_N -> Net-(U401-GPIO36)
- R412 pad 2: Net-(U401-GPIO42/ADC2) -> /FT232H_SS_N
- R413 pad 1: /FT232H_MISO -> Net-(U401-GPIO35)
- R413 pad 2: Net-(U401-GPIO43/ADC3) -> /FT232H_MISO
- R414 pad 1: /LOGIC_ANALYZER_MARKER0 -> Net-(U401-GPIO33)
- R414 pad 2: Net-(U401-GPIO44/ADC4) -> /LOGIC_ANALYZER_MARKER0
- R415 pad 1: /LOGIC_ANALYZER_MARKER1 -> Net-(U401-GPIO32)
- R415 pad 2: Net-(U401-GPIO45/ADC5) -> /LOGIC_ANALYZER_MARKER1
- R418 pad 1: /rp2350/GPIO36 -> /rp2350/GPIO42
- R419 pad 1: /rp2350/GPIO36 -> /rp2350/GPIO42
- R420 pad 1: /rp2350/GPIO37 -> /rp2350/GPIO43
- R421 pad 1: /rp2350/GPIO37 -> /rp2350/GPIO43
- R422 pad 1: /rp2350/GPIO38 -> /rp2350/GPIO44
- R423 pad 1: /rp2350/GPIO38 -> /rp2350/GPIO44
- R424 pad 1: /rp2350/GPIO39 -> /rp2350/GPIO45
- R425 pad 1: /rp2350/GPIO39 -> /rp2350/GPIO45
- R426 pad 1: /rp2350/GPIO40 -> /rp2350/GPIO34
- R427 pad 1: /rp2350/GPIO40 -> /rp2350/GPIO34
- U401 pad 43: Net-(U401-GPIO34) -> /rp2350/GPIO34
- U401 pad 45: /rp2350/GPIO36 -> Net-(U401-GPIO36)
- U401 pad 46: /rp2350/GPIO37 -> Net-(U401-GPIO37)
- U401 pad 47: /rp2350/GPIO38 -> Net-(U401-GPIO38)
- U401 pad 48: /rp2350/GPIO39 -> Net-(U401-GPIO39)
- U401 pad 49: /rp2350/GPIO40 -> Net-(U401-GPIO40/ADC0)
- U401 pad 53: Net-(U401-GPIO42/ADC2) -> /rp2350/GPIO42
- U401 pad 54: Net-(U401-GPIO43/ADC3) -> /rp2350/GPIO43
- U401 pad 55: Net-(U401-GPIO44/ADC4) -> /rp2350/GPIO44
- U401 pad 56: Net-(U401-GPIO45/ADC5) -> /rp2350/GPIO45
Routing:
- net /I2C_SDA: track 0.00 -> 58.0 mm, vias 0 -> 2
- net /I2C_SCL: track 0.00 -> 56.6 mm, vias 0 -> 2
- net /FT232H_MIOSIO0: track 0.00 -> 39.3 mm, vias 0 -> 2
- net /FT232H_MIOSIO2: track 0.00 -> 36.3 mm, vias 0 -> 2
- net /FT232H_MIOSIO1: track 0.00 -> 35.9 mm, vias 0 -> 2
- net /FT232H_SS_N: track 0.00 -> 34.4 mm
- net /FT232H_MISO: track 0.00 -> 33.8 mm
- net /FT232H_MIOSIO3: track 0.00 -> 33.0 mm, vias 0 -> 2
- net /FT232H_SCLK: track 0.00 -> 32.8 mm
- net /FT232H_WRITE_INVERTED: track 0.00 -> 32.3 mm
- net /rp2350/GPIO42: track 0.00 -> 25.5 mm
- net /rp2350/GPIO43: track 0.00 -> 22.2 mm
- net /SD_D0: track 0.00 -> 19.7 mm, vias 0 -> 2
- net /rp2350/GPIO44: track 0.00 -> 19.5 mm
- net /SD_CMD: track 0.00 -> 18.4 mm, vias 0 -> 2
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
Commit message: L3 power pours
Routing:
- added copper zone on In2.Cu, net +5V_SYS
- added copper zone on In2.Cu, net TERMPWR
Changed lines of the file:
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@@
+	)
+	(zone
+		(net 2)
+		(net_name "+5V_SYS")
+		(layer "In2.Cu")
+		(name "L3 +5V_SYS west-edge power-entry pour")
+		(hatch edge 0.5)
+		(priority 1)
+		(connect_pads yes
+			(clearance 0.2)
+		)
+		(min_thickness 0.2)
+		(filled_areas_thickness no)
+		(fill yes
+			(thermal_gap 0.5)
+			(thermal_bridge_width 0.5)
+		)
+		(polygon
+			(pts
+				(xy 99.95 29.95) (xy 112 29.95) (xy 112 120.05) (xy 99.95 120.05)
+			)
+		)
 	)
 	(zone
@@
 			)
 		)
+	)
+	(zone
+		(net 244)
+		(net_name "TERMPWR")
+		(layer "In2.Cu")
+		(name "L3 TERMPWR south + east-edge pour")
+		(hatch edge 0.5)
+		(priority 1)
+		(connect_pads yes
+			(clearance 0.2)
+		)
+		(min_thickness 0.2)
+		(filled_areas_thickness no)
+		(fill yes
+			(thermal_gap 0.5)
+			(thermal_bridge_width 0.5)
+		)
+		(polygon
+			(pts
+				(xy 130 105) (xy 208.31 105) (xy 208.31 46.774) (xy 220.05 46.774) (xy 220.05 120.05) (xy 130 120.05)
+			)
+		)
